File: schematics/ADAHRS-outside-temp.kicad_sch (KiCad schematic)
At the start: 24 parts, among them J1 Connector_PinHeader_2.54mm:Pi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, U1 LM2776, U2 OPA197xDBV, U3 OPA197xDBV, U4 LM2776

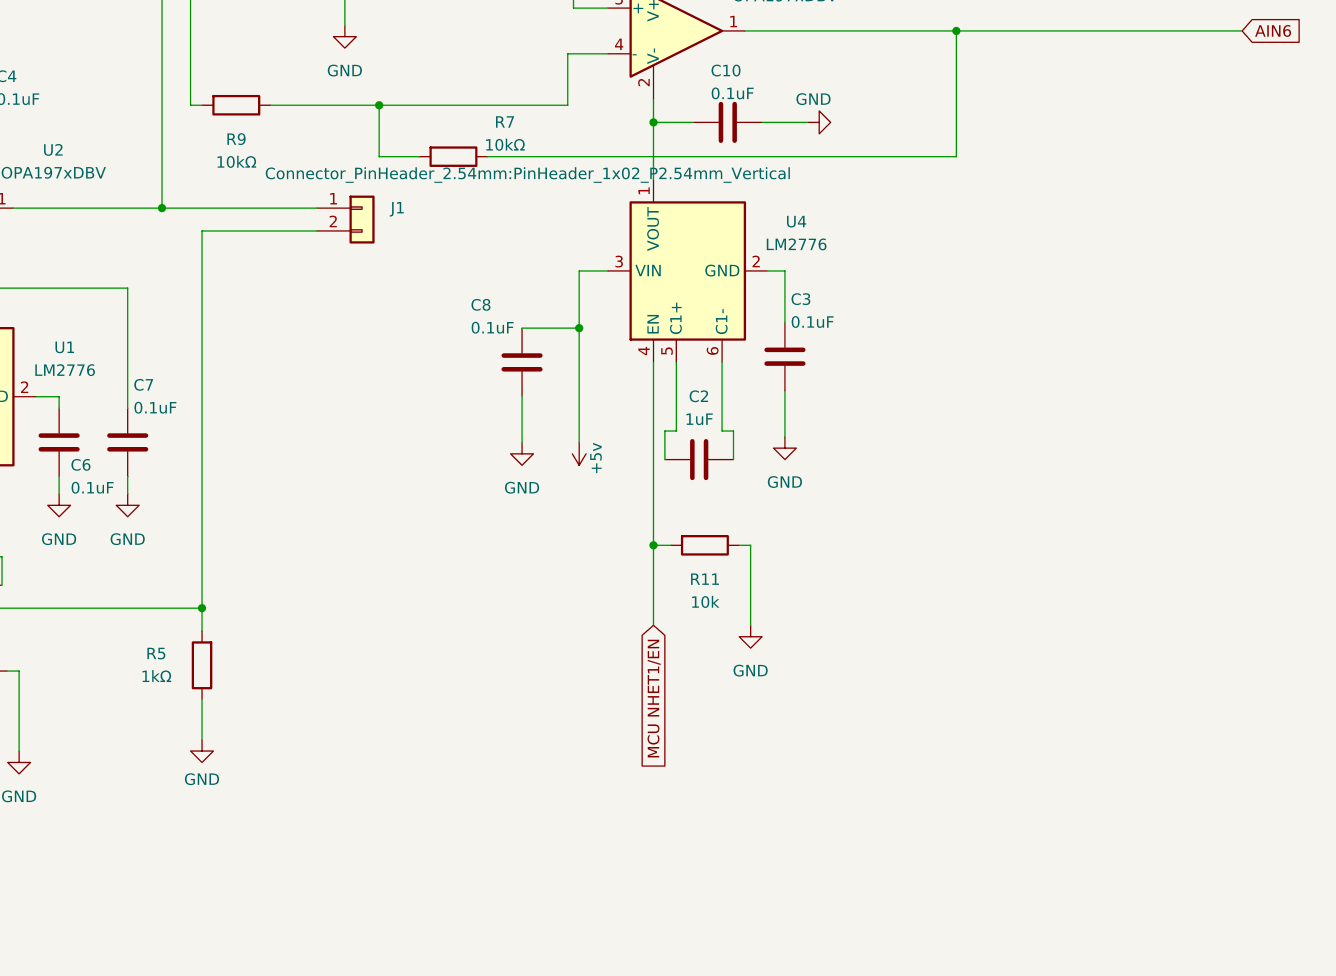
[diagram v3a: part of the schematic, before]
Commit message: Added molex connectors v1.04
I did not want to use actual pin headers because, that would have easily not have been passed through the FAA. It was only used as a stand in when I find the actual part. I could not find a symbol due to these mainly being generic but I did find the footprint so I added it for the pin header.
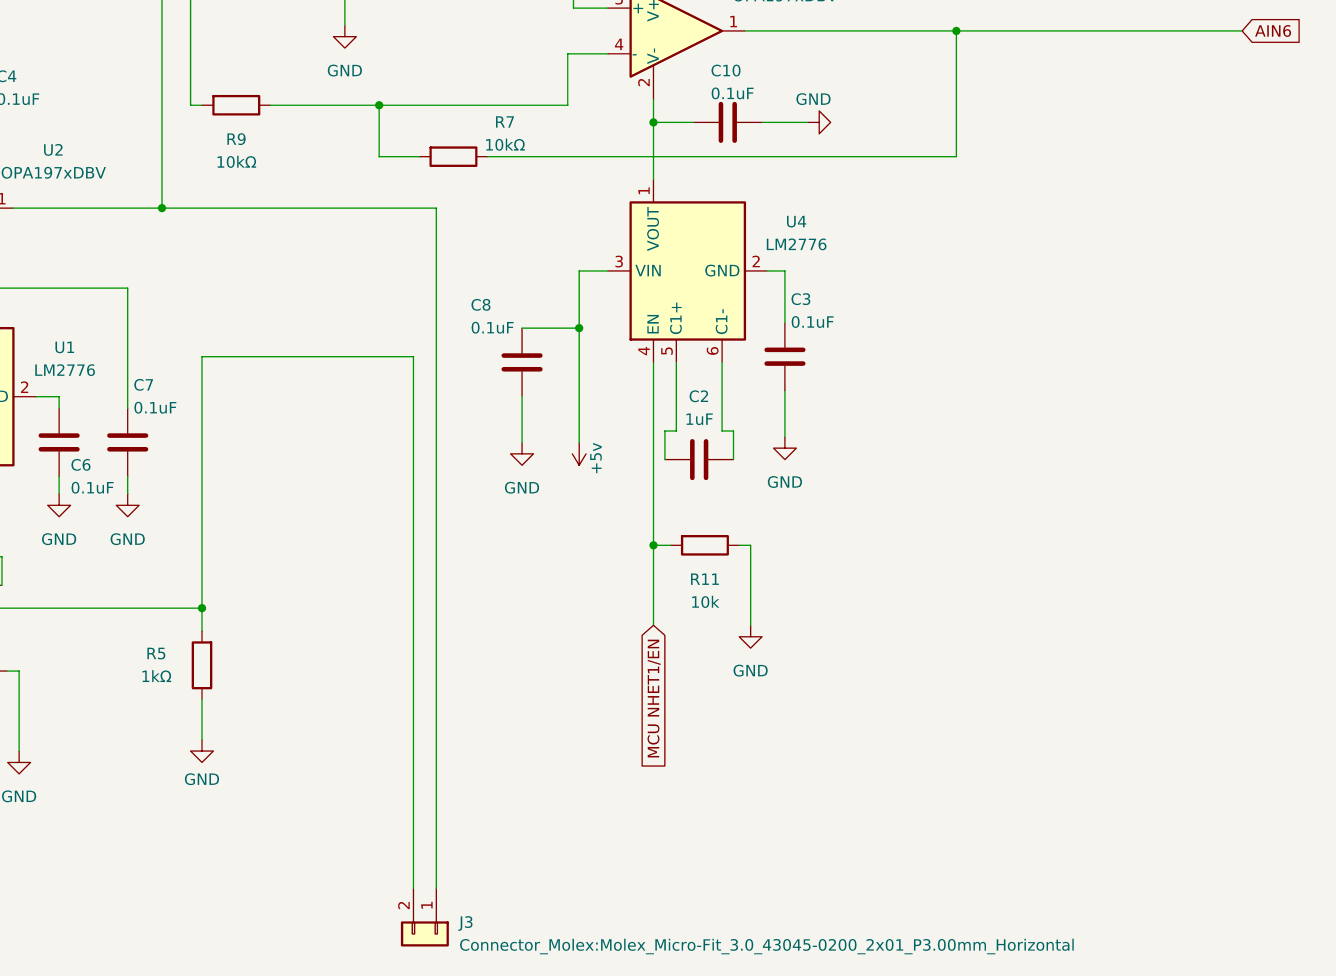
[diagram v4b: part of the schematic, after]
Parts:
- removed J1: Connector_PinHeader_2.54mm:PinHeader_1x02_P2.54mm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, symbol Connector_Generic:Conn_01x02
- added J3: Connector_Molex:Molex_Micro-Fit_3.0_43045-0200_2x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, Connector_Molex:Molex_Micro-Fit_3.0_43045-0200_2x01_P3.00mm_Horizontal, symbol Connector_Generic:Conn_01x02
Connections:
- net at R6.2, U2.1: now also J3.1 (Pin_1)
- net at R5.2, U2.4 (-): now also J3.2 (Pin_2)
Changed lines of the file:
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@@
-	(wire
-		(pts
-			(xy 123.825 79.375) (xy 123.825 121.285)
-		)
-		(stroke
-			(width 0)
-			(type default)
-		)
-	)
 	(wire
 		(pts
@@
 	(wire
 		(pts
+			(xy 147.32 93.345) (xy 147.32 152.4)
+		)
+		(stroke
+			(width 0)
+			(type default)
+		)
+	)
+	(wire
+		(pts
 			(xy 107.95 99.06) (xy 107.95 97.79)
 		)
@@
 	(wire
 		(pts
-			(xy 119.38 76.835) (xy 136.525 76.835)
+			(xy 119.38 76.835) (xy 149.86 76.835)
 		)
 		(stroke
@@
 	(wire
 		(pts
+			(xy 149.86 76.835) (xy 149.86 152.4)
+		)
+		(stroke
+			(width 0)
+			(type default)
+		)
+	)
+	(wire
+		(pts
 			(xy 95.25 107.95) (xy 95.25 115.57)
 		)
@@
 	(wire
 		(pts
-			(xy 123.825 79.375) (xy 136.525 79.375)
-		)
-		(stroke
-			(width 0)
-			(type default)
-		)
-	)
-	(wire
-		(pts
 			(xy 100.33 115.57) (xy 101.6 115.57)
 		)
@@
 	(wire
 		(pts
+			(xy 123.825 93.345) (xy 123.825 121.285)
+		)
+		(stroke
+			(width 0)
+			(type default)
+		)
+	)
+	(wire
+		(pts
 			(xy 92.71 107.95) (xy 92.71 128.27)
 		)
@@
 		(pts
 			(xy 84.455 84.455) (xy 84.455 86.995)
+		)
+		(stroke
+			(width 0)
+			(type default)
+		)
+	)
+	(wire
+		(pts
+			(xy 123.825 93.345) (xy 147.32 93.345)
 		)
 		(stroke
@@
 	)
 	(symbol
+		(lib_id "Connector_Generic:Conn_01x02")
+		(at 149.86 157.48 270)
+		(unit 1)
+		(exclude_from_sim no)
+		(in_bom yes)
+		(on_board yes)
+		(dnp no)
+		(fields_autoplaced yes)
+		(property "Reference" "J3"
+			(at 152.4 156.2099 90)
+			(effects
+				(font
+					(size 1.27 1.27)
+				)
+				(justify left)
+			)
+		)
+		(property "Value" "Connector_Molex:Molex_Micro-Fit_3.0_43045-0200_2x01_P3.00mm_Horizontal"
+			(at 152.4 158.7499 90)
+			(effects
+				(font
+					(size 1.27 1.27)
+				)
+				(justify left)
+			)
+		)
+		(property "Footprint" "Connector_Molex:Molex_Micro-Fit_3.0_43045-0200_2x01_P3.00mm_Horizontal"
+			(at 149.86 157.48 0)
+			(effects
+				(font
+					(size 1.27 1.27)
+				)
+				(hide yes)
+			)
+		)
+		(property "Datasheet" "~"
+			(at 149.86 157.48 0)
+			(effects
+				(font
+					(size 1.27 1.27)
+				)
+				(hide yes)
+			)
+		)
+		(property "Description" "Generic connector, single row, 01x02, script generated (kicad-library-utils/schlib/autogen/connector/)"
+			(at 149.86 157.48 0)
+			(effects
+				(font
+					(size 1.27 1.27)
+				)
+				(hide yes)
+			)
+		)
+		(pin "1"
+		)
+		(pin "2"
+		)
+		(instances
+			(project "ADAHRS-outside-temp"
+				(path "/1c9d1702-4215-4f0e-92e0-1fbfd28a9266"
+					(reference "J3")
+					(unit 1)
+				)
+			)
+		)
+	)
+	(symbol
 		(lib_id "power:GND")
 		(at 139.7 56.515 0)
@@
 					(unit 1)
 				)
-			)
-		)
-	)
-	(symbol
-		(lib_id "Connector_Generic:Conn_01x02")
-		(at 141.605 76.835 0)
-		(unit 1)
-		(exclude_from_sim no)
-		(in_bom yes)
-		(on_board yes)
-		(dnp no)
-		(property "Reference" "J1"
-			(at 144.78 76.8349 0)
-			(effects
-				(font
-					(size 1.27 1.27)
-				)
-				(justify left)
-			)
-		)
-		(property "Value" "Connector_PinHeader_2.54mm:PinHeader_1x02_P2.54mm_Vertical"
-			(at 130.81 73.025 0)
-			(effects
-				(font
-					(size 1.27 1.27)
-				)
-				(justify left)
-			)
-		)
-		(property "Footprint" ""
-			(at 141.605 76.835 0)
-			(effects
-				(font
-					(size 1.27 1.27)
-				)
-				(hide yes)
-			)
-		)
-		(property "Datasheet" "~"
-			(at 141.605 76.835 0)
-			(effects
-				(font
-					(size 1.27 1.27)
-				)
-				(hide yes)
-			)
-		)
-		(property "Description" "Generic connector, single row, 01x02, script generated (kicad-library-utils/schlib/autogen/connector/)"
-			(at 141.605 76.835 0)
-			(effects
-				(font
-					(size 1.27 1.27)
-				)
-				(hide yes)
-			)
-		)
-		(pin "1"
-		)
-		(pin "2"
-		)
-		(instances
-			(project ""
-				(path "/1c9d1702-4215-4f0e-92e0-1fbfd28a9266"
-					(reference "J1")
-					(unit 1)
-				)

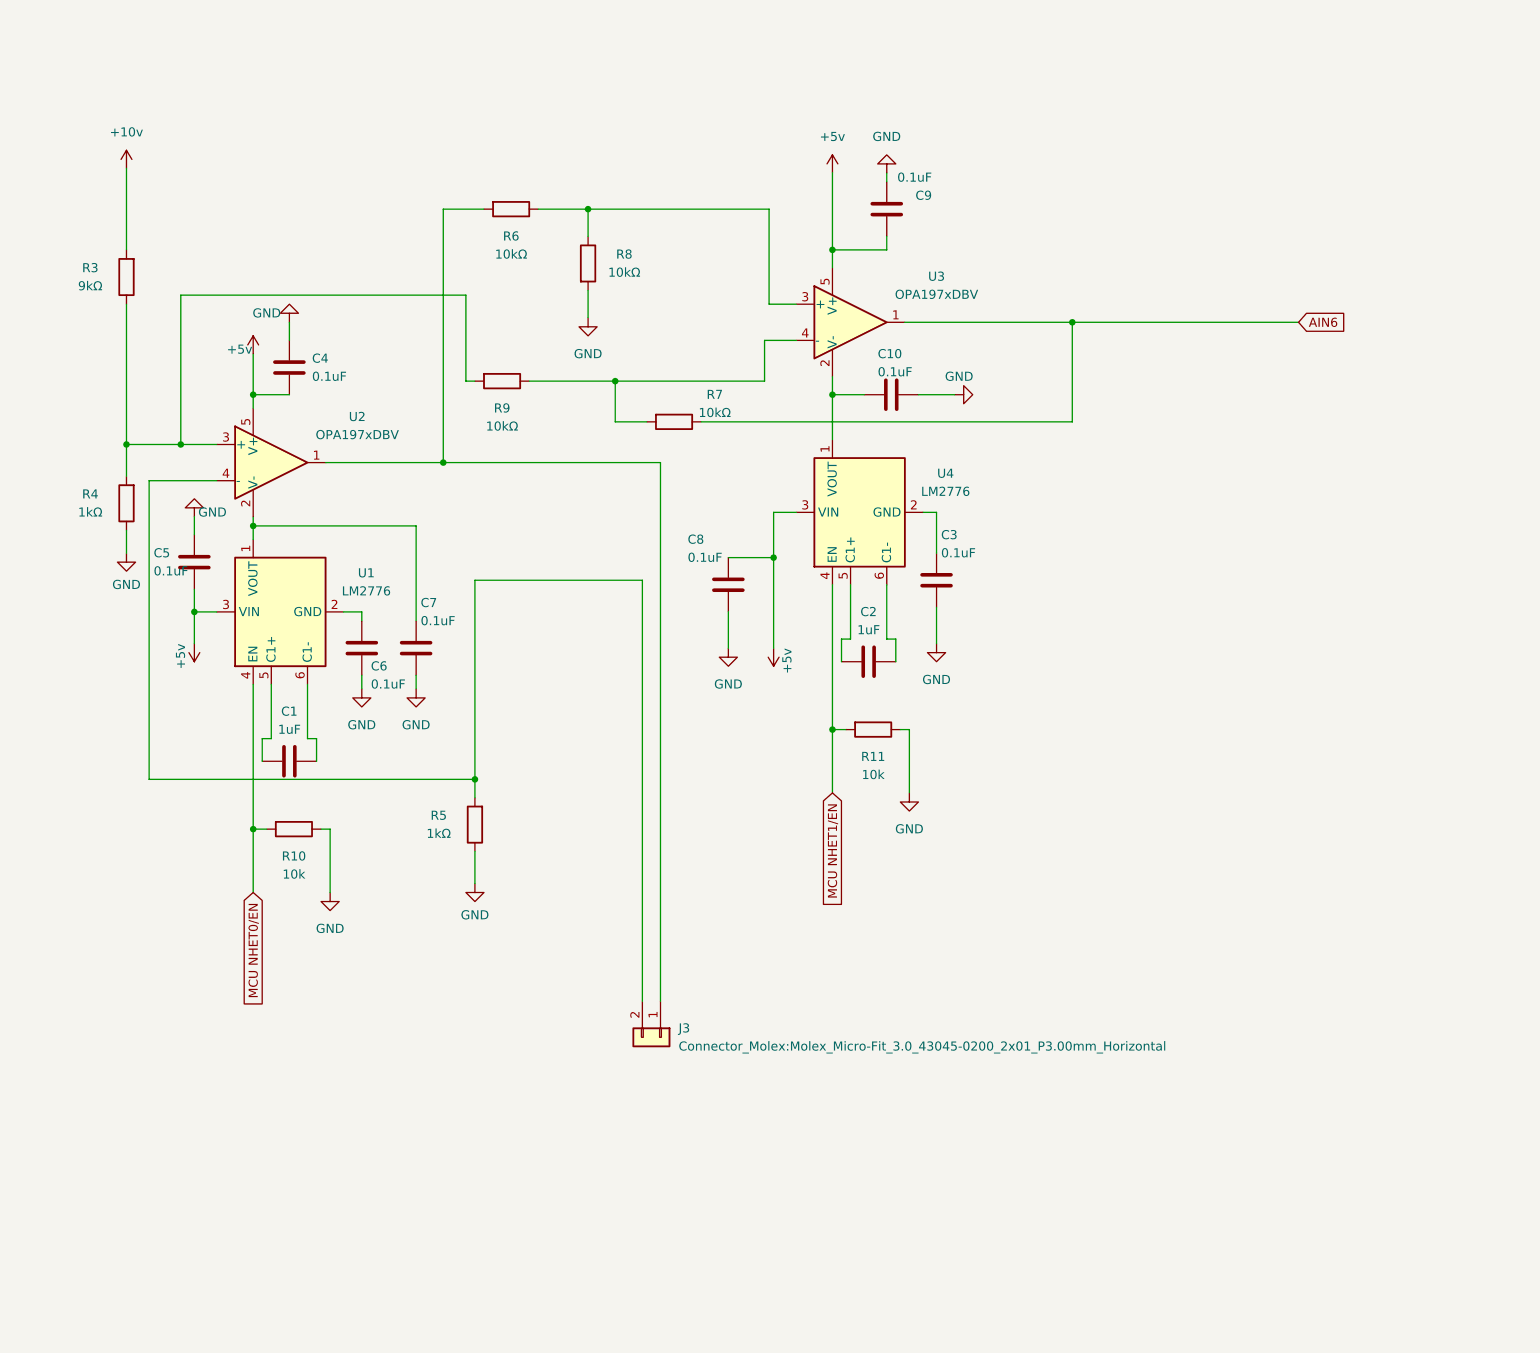
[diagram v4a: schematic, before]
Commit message: switch regulator (-5v) temp v1.05
I simplified the wiring diagram. It is not necessary to have 2 switch regulators.
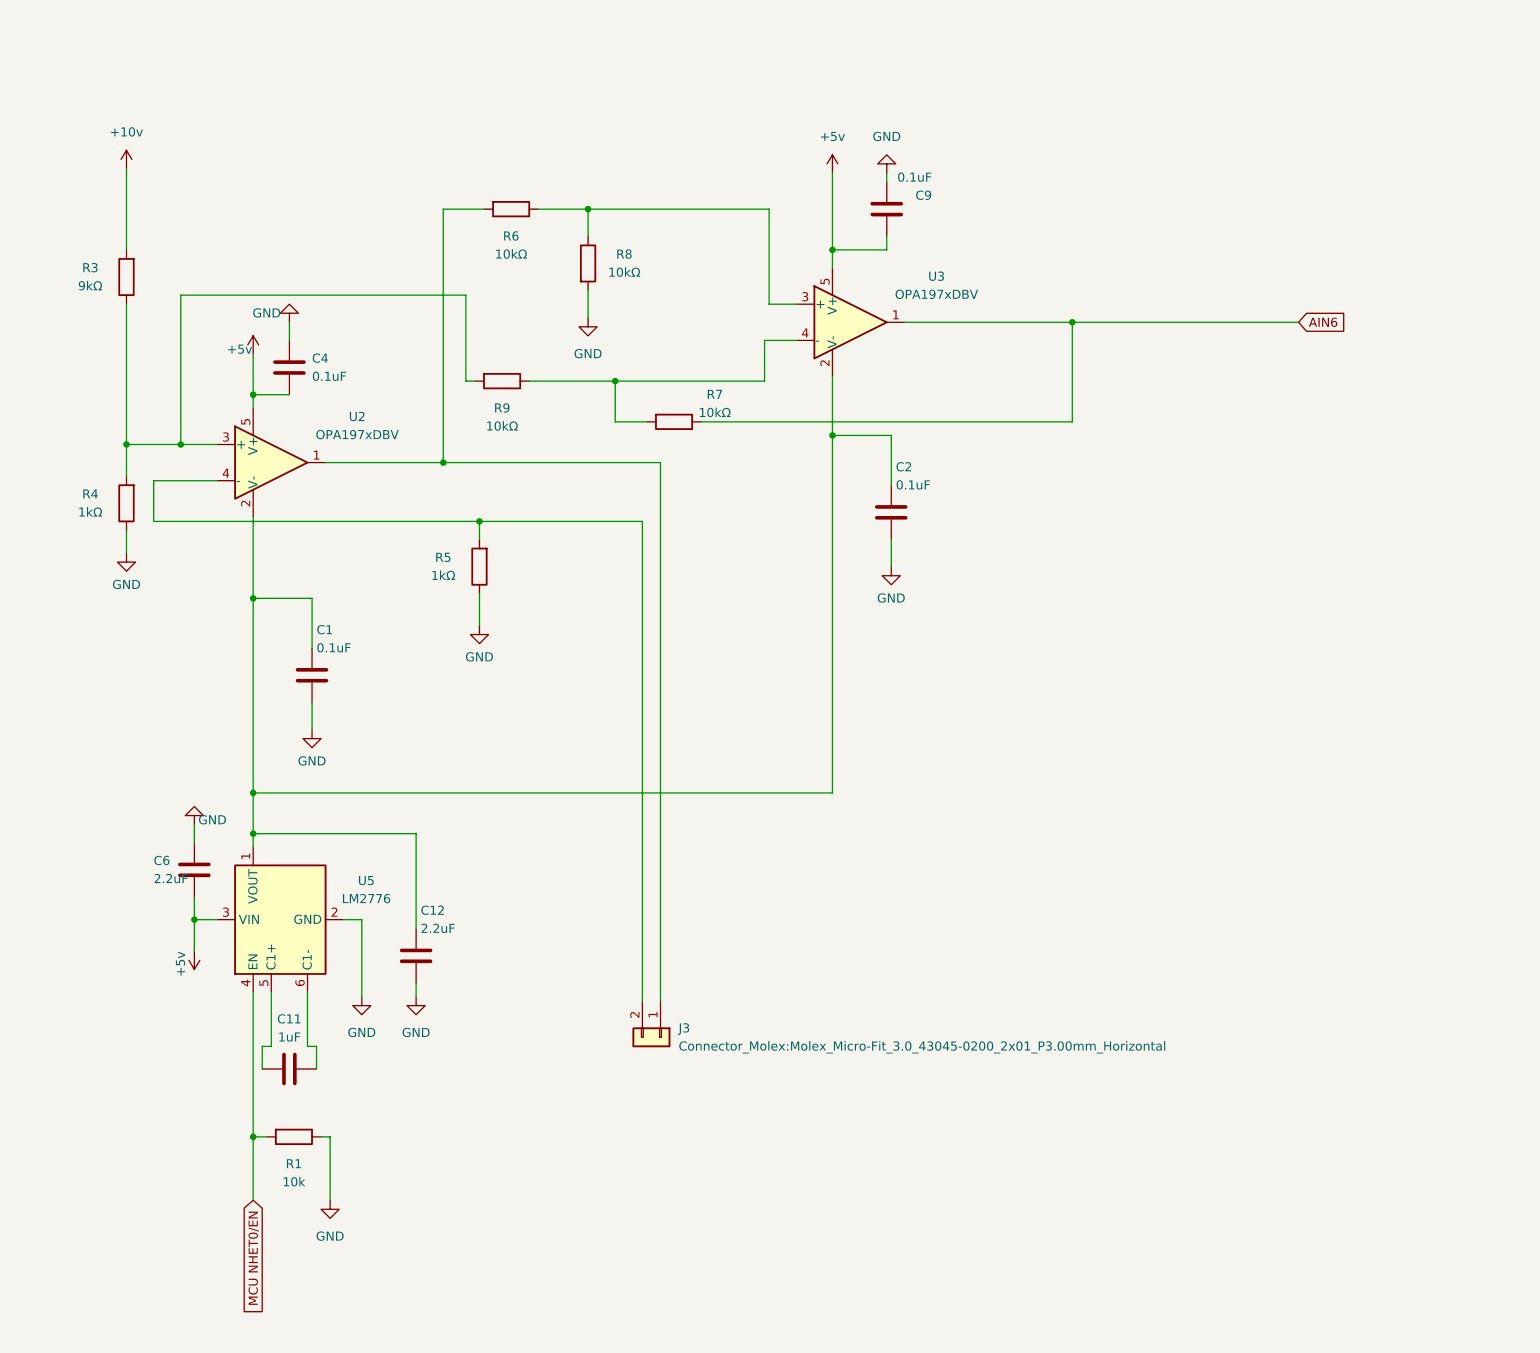
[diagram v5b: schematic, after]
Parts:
- removed C10, C3, C5, C7, C8: 0.1uF, symbol Device:C
- removed R10, R11: 10k, symbol Device:R
- removed U1, U4: LM2776, Package_TO_SOT_SMD:SOT-23-6, symbol Regulator_SwitchedCapacitor:LM2776
- added C11: 1uF, symbol Device:C
- added C12: 2.2uF, symbol Device:C
- added R1: 10k, symbol Device:R
- added U5: LM2776, Package_TO_SOT_SMD:SOT-23-6, symbol Regulator_SwitchedCapacitor:LM2776
- C1, C2: value 1uF -> 0.1uF
- C6: value 0.1uF -> 2.2uF
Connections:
- net +5v: now also C6.1, U5.3 (VIN)
- net GND: now also C1.1, C2.1, C6.2, C12.1, R1.1, U5.2 (GND); no longer C6.1
- net MCU NHET0/EN: now also R1.2, U5.4 (EN)
- net at C1.2: now also C2.2, U2.2 (V-), U3.2 (V-), C12.2, U5.1 (VOUT)
- new net: C11.1, U5.5 (C1+)
- new net: C11.2, U5.6 (C1-)
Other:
- moved on the sheet: R5
